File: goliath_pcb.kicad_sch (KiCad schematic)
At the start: 31 parts, among them IC1 MCT9001SD, IC2 MCT9001SD, IC3 MCT9001SD, IC4 MCT9001SD, IC5 MCT9001SD, J1 RJ45_LED, J2 RJ45_LED, Q5 BSS138, U1 Pico

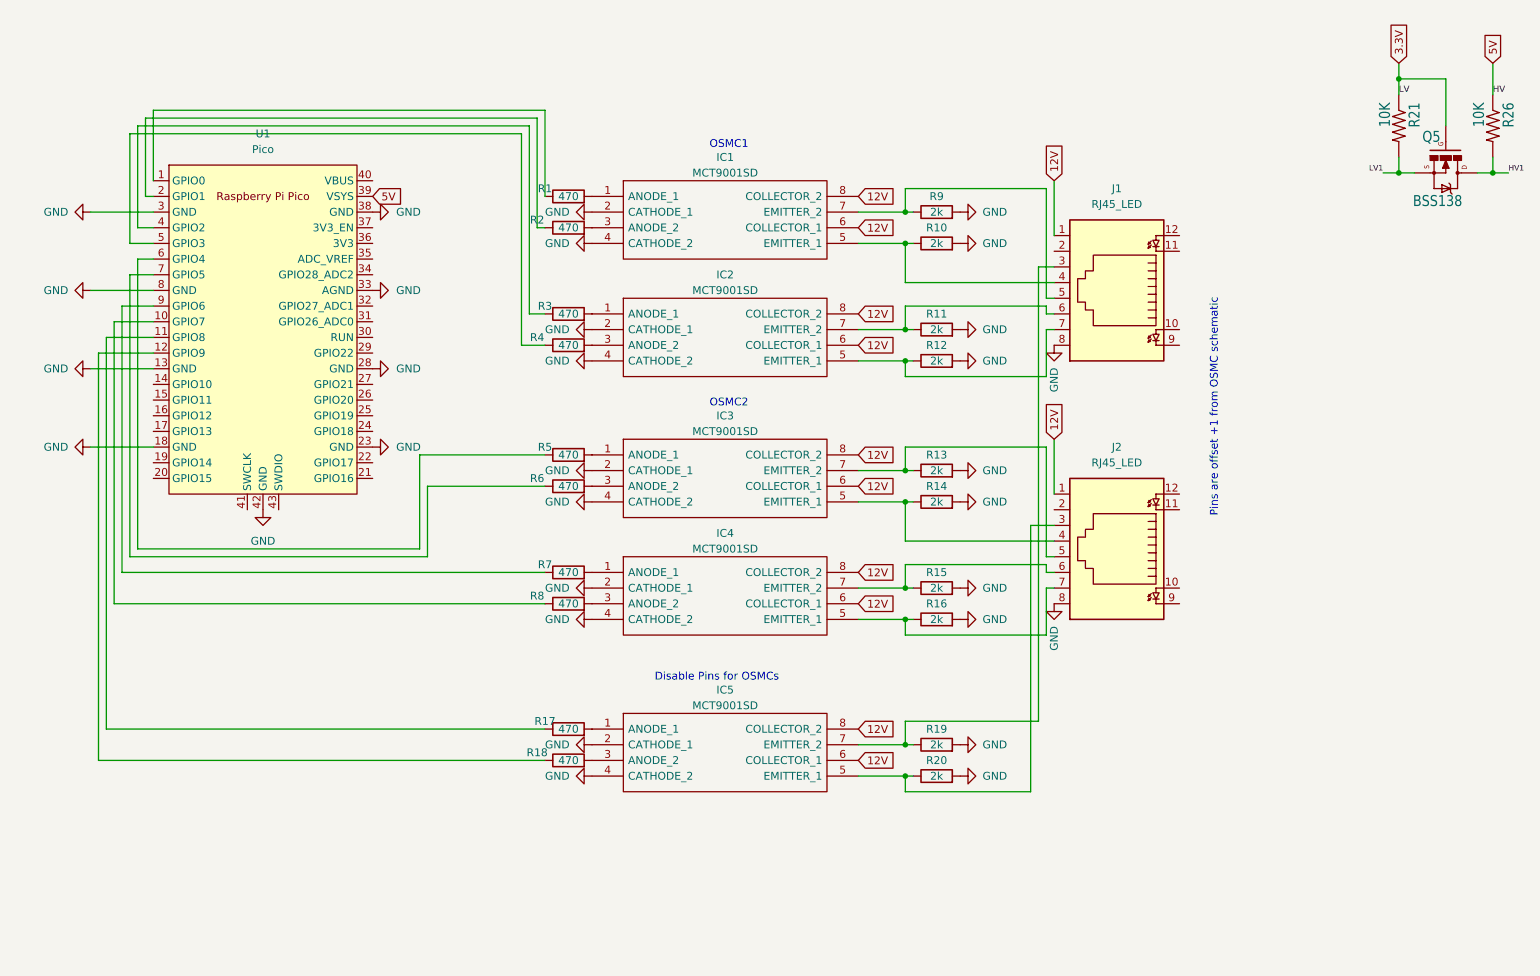
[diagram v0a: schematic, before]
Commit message: Add ADC for battery monitoring
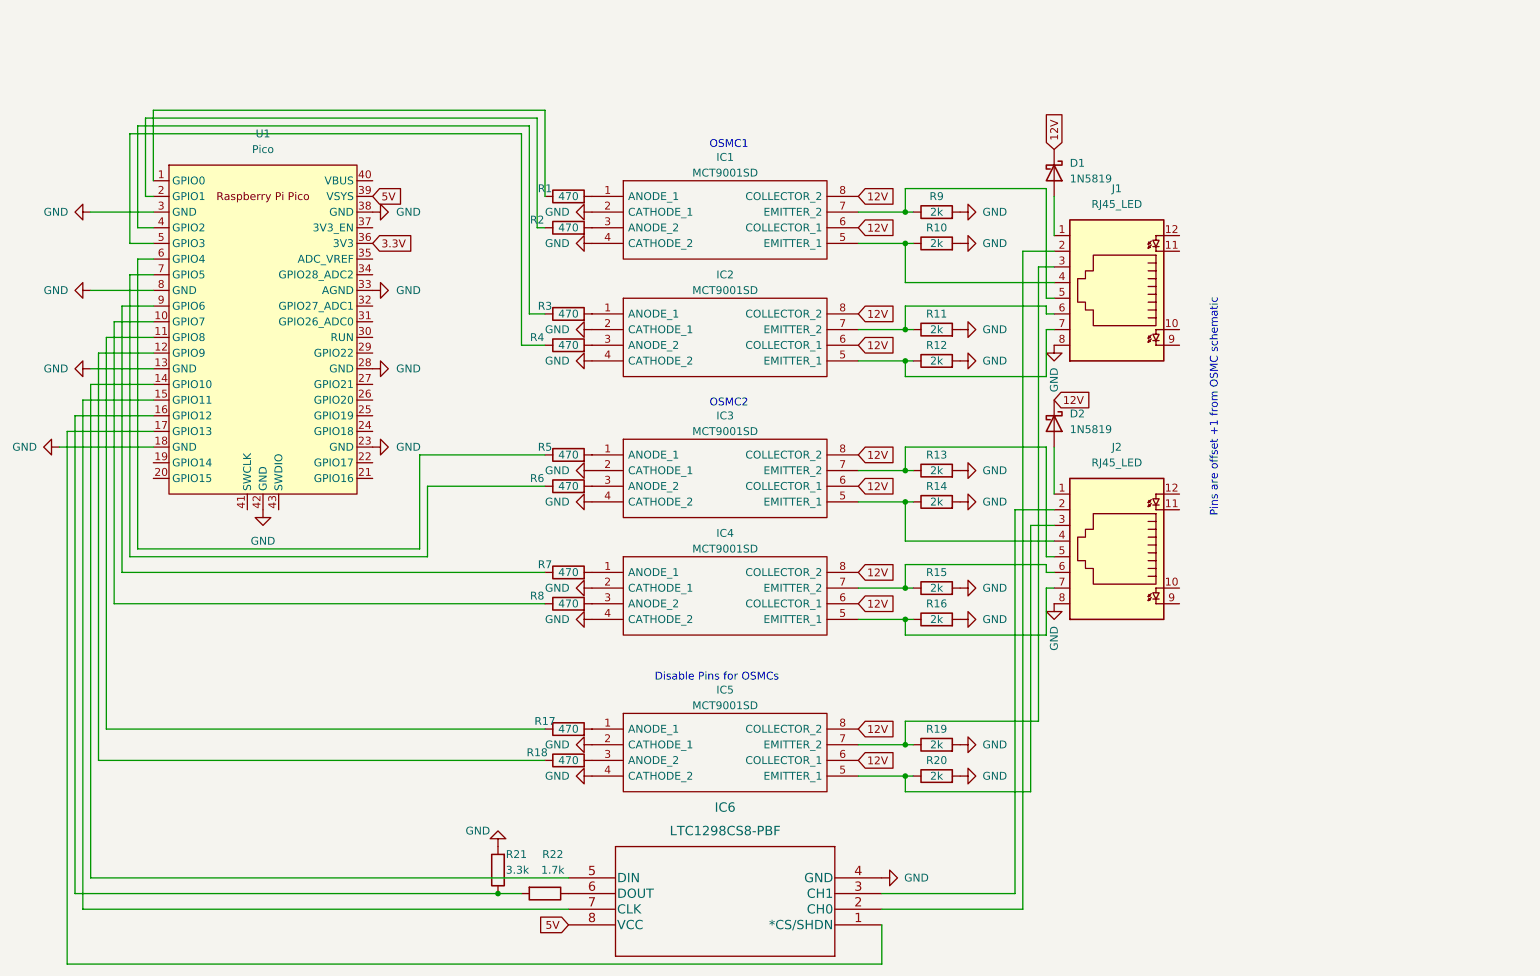
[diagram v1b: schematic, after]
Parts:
- removed Q5: BSS138, Logic_Level_Bidirectional:SOT23-3, symbol Logic_Level_Bidirectional-eagle-import:MOSFET-NCHANNELSMD
- removed R21, R26: 10K, Resistor_THT:R_Axial_DIN0207_L6.3mm_D2.5mm_P10.16mm_Horizontal, symbol Logic_Level_Bidirectional-eagle-import:RESISTOR0603-RES
- added D1, D2: 1N5819, Diode_THT:D_DO-41_SOD81_P10.16mm_Horizontal, symbol Diode:1N5819
- added IC6: LTC1298CS8-PBF, SO-8_S_LIT, symbol LTC1298:LTC1298CS8-PBF
- added R21: 3.3k, symbol Device:R
- added R22: 1.7k, symbol Device:R
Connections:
- net 12V: now also D1.1 (K), D2.1 (K); no longer J1.1, J2.1
- net 3.3V: now also U1.36 (3V3)
- net 5V: now also IC6.8 (VCC)
- net GND: now also IC6.4 (GND), R21.2
- net at J1.2: now also IC6.2 (CH0)
- net at J2.2: now also IC6.3 (CH1)
- net at U1.14 (GPIO10): now also IC6.5 (DIN)
- net at U1.15 (GPIO11): now also IC6.7 (CLK)
- net at U1.16 (GPIO12): now also R21.1, R22.2
- net at U1.17 (GPIO13): now also IC6.1 (*CS/SHDN)
- new net: IC6.6 (DOUT), R22.1
- new net: D2.2 (A), J2.1
- new net: D1.2 (A), J1.1

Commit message: Add LTC1798 ADC on PCB
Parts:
- IC6: footprint SO-8_S_LIT -> footprints:LTC1298CS8-PBF
- R21, R22: footprint (none) -> Resistor_THT:R_Axial_DIN0207_L6.3mm_D2.5mm_P10.16mm_Horizontal
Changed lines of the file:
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@@
       (effects (font (size 1.524 1.524)))
     )
-    (property "Footprint" "SO-8_S_LIT" (id 2) (at 129.54 168.656 0)
+    (property "Footprint" "footprints:LTC1298CS8-PBF" (id 2) (at 129.54 168.656 0)
       (effects (font (size 1.524 1.524)) hide)
     )
@@
       (effects (font (size 1.27 1.27)) (justify right))
     )
-    (property "Footprint" "" (id 2) (at 94.488 153.67 90)
+    (property "Footprint" "Resistor_THT:R_Axial_DIN0207_L6.3mm_D2.5mm_P10.16mm_Horizontal" (id 2) (at 94.488 153.67 90)
       (effects (font (size 1.27 1.27)) hide)
     )
@@
     (property "Reference" "R22" (id 0) (at 101.6 151.13 90))
     (property "Value" "1.7k" (id 1) (at 101.6 153.67 90))
-    (property "Footprint" "" (id 2) (at 100.33 155.702 90)
+    (property "Footprint" "Resistor_THT:R_Axial_DIN0207_L6.3mm_D2.5mm_P10.16mm_Horizontal" (id 2) (at 100.33 155.702 90)
       (effects (font (size 1.27 1.27)) hide)
     )
@@
     )
     (path "/24e72518-d87c-4a77-a932-4000c7b6be55"
-      (reference "IC6") (unit 1) (value "LTC1298CS8-PBF") (footprint "SO-8_S_LIT")
+      (reference "IC6") (unit 1) (value "LTC1298CS8-PBF") (footprint "footprints:LTC1298CS8-PBF")
     )
     (path "/47e07bf5-f704-4a6a-8706-99bf0d77d2a8"
@@
     )
     (path "/6de4532b-e9e0-4a36-b9b7-cc0ceb1559fe"
-      (reference "R21") (unit 1) (value "3.3k") (footprint "")
+      (reference "R21") (unit 1) (value "3.3k") (footprint "Resistor_THT:R_Axial_DIN0207_L6.3mm_D2.5mm_P10.16mm_Horizontal")
     )
     (path "/e4f98602-ff42-406f-aff2-6aab18d58ebb"
-      (reference "R22") (unit 1) (value "1.7k") (footprint "")
+      (reference "R22") (unit 1) (value "1.7k") (footprint "Resistor_THT:R_Axial_DIN0207_L6.3mm_D2.5mm_P10.16mm_Horizontal")
     )
     (path "/cb20d2a1-05a5-401a-9981-368013b11a84"

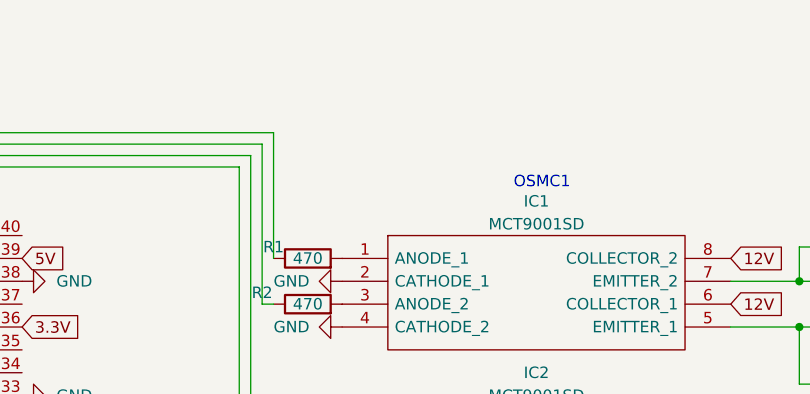
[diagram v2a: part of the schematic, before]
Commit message: Verify all connections, add 7805
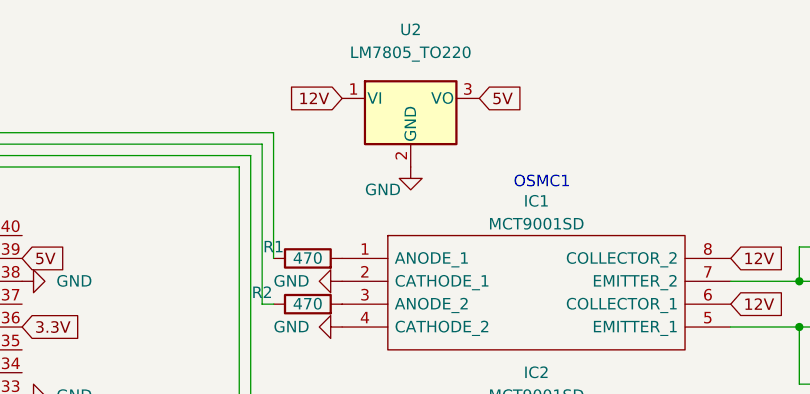
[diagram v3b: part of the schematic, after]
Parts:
- added U2: LM7805_TO220, Package_TO_SOT_THT:TO-220-3_Vertical, symbol Regulator_Linear:LM7805_TO220
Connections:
- net 12V: now also U2.1 (VI)
- net 5V: now also U2.3 (VO)
- net GND: now also U2.2 (GND)
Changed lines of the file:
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@@
+    )
+  )
+  (global_label "12V" (shape input) (at 107.95 26.67 180) (fields_autoplaced)
+    (effects (font (size 1.27 1.27)) (justify right))
+    (property "Intersheet References" "${INTERSHEET_REFS}" (id 0) (at 102.0293 26.5906 0)
+      (effects (font (size 1.27 1.27)) (justify right) hide)
+    )
+  )
+  (global_label "5V" (shape input) (at 123.19 26.67 0) (fields_autoplaced)
+    (effects (font (size 1.27 1.27)) (justify left))
+    (property "Intersheet References" "${INTERSHEET_REFS}" (id 0) (at 127.9012 26.5906 0)
+      (effects (font (size 1.27 1.27)) (justify left) hide)
     )
   )
@@
     (pin "2")
   )
+  (symbol (lib_id "Regulator_Linear:LM7805_TO220") (at 115.57 26.67 0) (unit 1)
+    (in_bom yes) (on_board yes) (fields_autoplaced)
+    (property "Reference" "U2" (id 0) (at 115.57 19.05 0))
+    (property "Value" "LM7805_TO220" (id 1) (at 115.57 21.59 0))
+    (property "Footprint" "Package_TO_SOT_THT:TO-220-3_Vertical" (id 2) (at 115.57 20.955 0)
+      (effects (font (size 1.27 1.27) italic) hide)
+    )
+    (property "Datasheet" "https://www.onsemi.cn/PowerSolutions/document/MC7800-D.PDF" (id 3) (at 115.57 27.94 0)
+      (effects (font (size 1.27 1.27)) hide)
+    )
+    (pin "1")
+    (pin "2")
+    (pin "3")
+  )
   (symbol (lib_id "power:GND") (at 107.95 133.35 270) (unit 1)
     (in_bom yes) (on_board yes)
@@
     )
     (property "Datasheet" "" (id 3) (at 107.95 133.35 0)
+      (effects (font (size 1.27 1.27)) hide)
+    )
+    (pin "1")
+  )
+  (symbol (lib_id "power:GND") (at 115.57 34.29 0) (unit 1)
+    (in_bom yes) (on_board yes)
+    (property "Reference" "#PWR01" (id 0) (at 115.57 40.64 0)
+      (effects (font (size 1.27 1.27)) hide)
+    )
+    (property "Value" "GND" (id 1) (at 110.49 36.83 0)
+      (effects (font (size 1.27 1.27)) (justify left))
+    )
+    (property "Footprint" "" (id 2) (at 115.57 34.29 0)
+      (effects (font (size 1.27 1.27)) hide)
+    )
+    (property "Datasheet" "" (id 3) (at 115.57 34.29 0)
       (effects (font (size 1.27 1.27)) hide)
     )
@@
   )
   (symbol_instances
+    (path "/1b2f7cff-1ee0-4f27-b039-55be12b42e85"
+      (reference "#PWR01") (unit 1) (value "GND") (footprint "")
+    )
     (path "/20b3c90c-cd19-43ab-add4-d9614137be68"
       (reference "#PWR0101") (unit 1) (value "GND") (footprint "")
@@
       (reference "U1") (unit 1) (value "Pico") (footprint "MCU_RaspberryPi_and_Boards:RPi_Pico_SMD_TH")
     )
-  )
+    (path "/13a9b782-f91f-4f2c-87e2-727ffddd2d98"
+      (reference "U2") (unit 1) (value "LM7805_TO220") (footprint "Package_TO_SOT_THT:TO-220-3_Vertical")
+    )
+  )
